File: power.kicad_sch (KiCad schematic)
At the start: 19 parts, among them J1 USB_C_Receptacle_USB2.0_16P, U1 TLV62569DBV, U3 USBLC6-2SC6, U4 SPX3819M5-L-3-3

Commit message: MCU connected
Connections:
- net MCU_USB_D+: now reaches U3.4 (I/O2)
- net MCU_USB_D-: now reaches U3.6 (I/O1)
- net +3.3V renamed +3V3
- net +3.3VA renamed +3V3A
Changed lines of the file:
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@@
 	(rectangle
 		(start 13.97 80.01)
-		(end 96.52 153.035)
+		(end 104.14 153.035)
 		(stroke
 			(width 0.254)
@@
 	)
 	(rectangle
-		(start 99.06 14.605)
+		(start 105.41 14.605)
 		(end 284.48 161.925)
 		(stroke
@@
 	(wire
 		(pts
+			(xy 83.82 104.14) (xy 86.36 104.14)
+		)
+		(stroke
+			(width 0)
+			(type default)
+		)
+	)
+	(wire
+		(pts
 			(xy 207.01 142.24) (xy 166.37 142.24)
 		)
@@
 		(pts
 			(xy 52.07 116.84) (xy 69.85 116.84)
+		)
+		(stroke
+			(width 0)
+			(type default)
+		)
+	)
+	(wire
+		(pts
+			(xy 83.82 106.68) (xy 86.36 106.68)
 		)
 		(stroke
@@
 			)
 			(justify left bottom)
+		)
+	)
+	(global_label "MCU_USB_D-"
+		(shape input)
+		(at 86.36 104.14 0)
+		(fields_autoplaced yes)
+		(effects
+			(font
+				(size 1.27 1.27)
+			)
+			(justify left)
+		)
+		(property "Intersheetrefs" "${INTERSHEET_REFS}"
+			(at 101.9847 104.14 0)
+			(effects
+				(font
+					(size 1.27 1.27)
+				)
+				(justify left)
+				(hide yes)
+			)
+		)
+	)
+	(global_label "MCU_USB_D+"
+		(shape input)
+		(at 86.36 106.68 0)
+		(fields_autoplaced yes)
+		(effects
+			(font
+				(size 1.27 1.27)
+			)
+			(justify left)
+		)
+		(property "Intersheetrefs" "${INTERSHEET_REFS}"
+			(at 101.9847 106.68 0)
+			(effects
+				(font
+					(size 1.27 1.27)
+				)
+				(justify left)
+				(hide yes)
+			)
 		)
 	)
@@
 			)
 		)
-		(property "Value" "+3.3V"
-			(at 217.17 100.33 0)
-			(effects
-				(font
-					(size 1.27 1.27)
-				)
+		(property "Value" "+3V3"
+			(at 219.71 104.1399 0)
+			(effects
+				(font
+					(size 1.27 1.27)
+				)
+				(justify left)
 			)
 		)
@@
 			)
 		)
-		(property "Value" "+3.3VA"
+		(property "Value" "+3V3A"
 			(at 196.85 43.1799 0)
 			(effects

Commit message: adding anotations
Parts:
- renumbered U1 to U7
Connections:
- net +VBUS is gone; now on net VBUS: J1.A4 (VBUS), J1.A9 (VBUS), J1.B4 (VBUS), J1.B9 (VBUS), U3.5 (VBUS)
- net GND: now also C1.2, C2.2, C3.2, C6.2, U4.2 (GND)

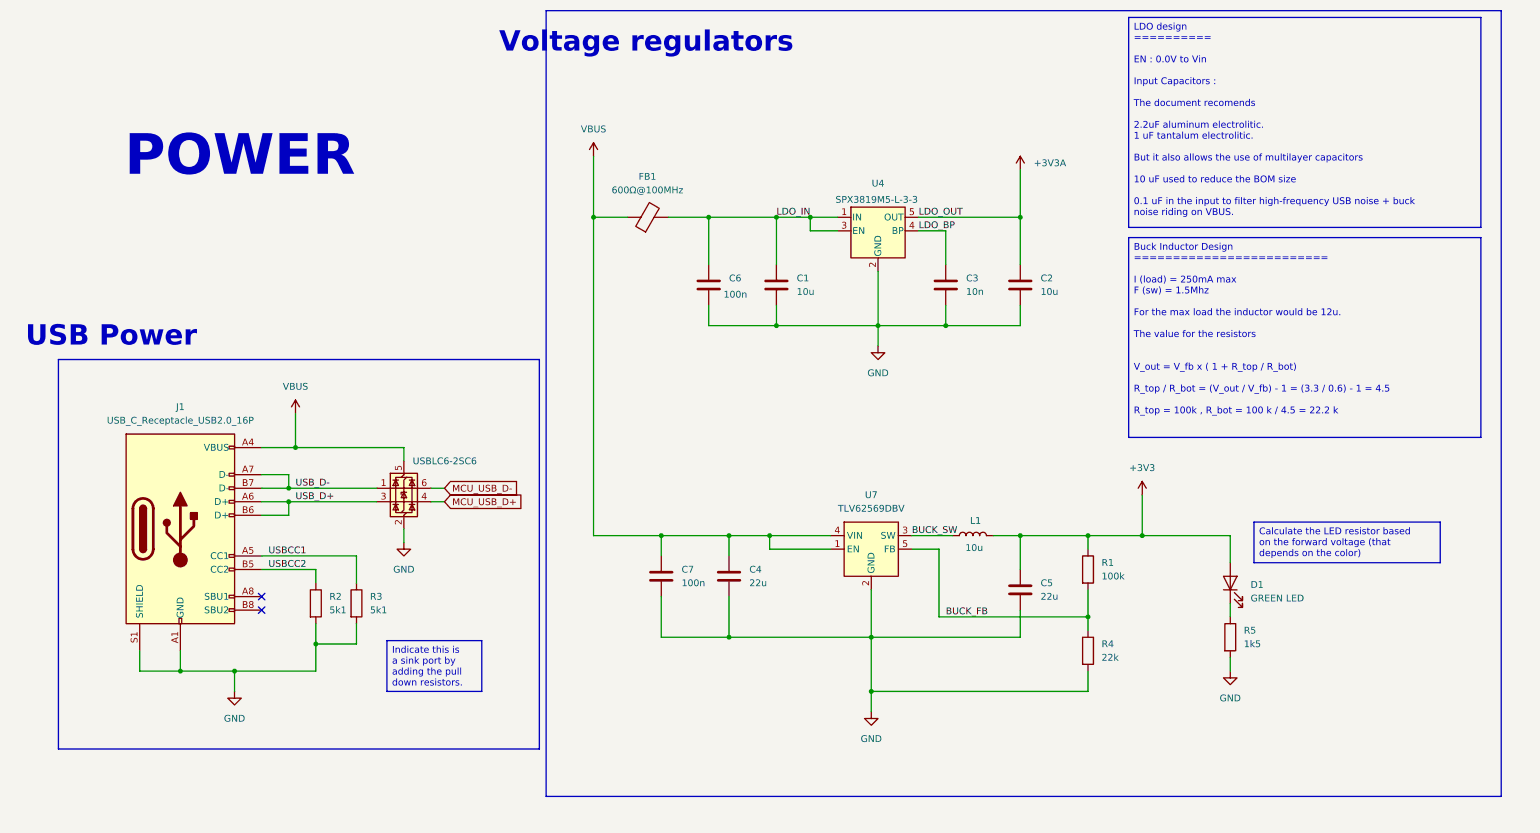
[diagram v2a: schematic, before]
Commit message: ERC fixed
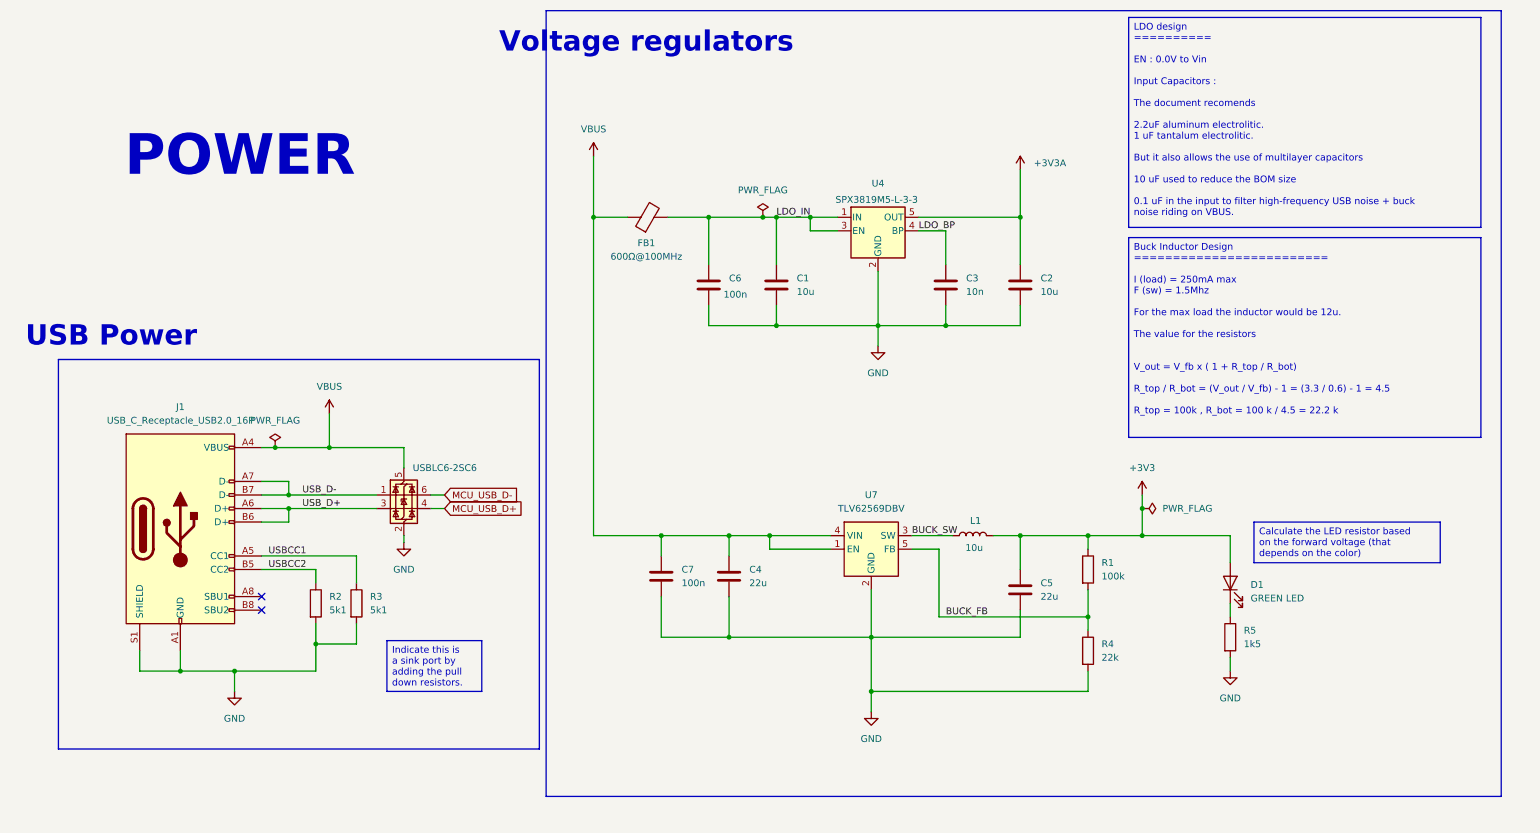
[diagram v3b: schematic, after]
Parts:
- removed J1: USB_C_Receptacle_USB2.0_16P, Connector_USB:USB_C_Receptacle_GCT_USB4105-xx-A_16P_TopMnt_Horizontal, symbol Connector:USB_C_Receptacle_USB2.0_16P
- added J1: USB_C_Receptacle_USB2.0_16P, Connector_USB:USB_C_Receptacle_GCT_USB4105-xx-A_16P_TopMnt_Horizontal, symbol Galerna:USB_C_Receptacle_USB2.0_16P
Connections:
- net GND: now also J1.A1 (GND), J1.A12 (GND), J1.B1 (GND), J1.B12 (GND), J1.S1 (SHIELD)
- net USBCC1: now also J1.A5 (CC1)
- net USBCC2: now also J1.B5 (CC2)
- net USB_D+: now also J1.A6 (D+), J1.B6 (D+)
- net USB_D-: now also J1.A7 (D-), J1.B7 (D-)
- net VBUS: now also J1.A4 (VBUS), J1.A9 (VBUS), J1.B4 (VBUS), J1.B9 (VBUS)

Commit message: footprints updated
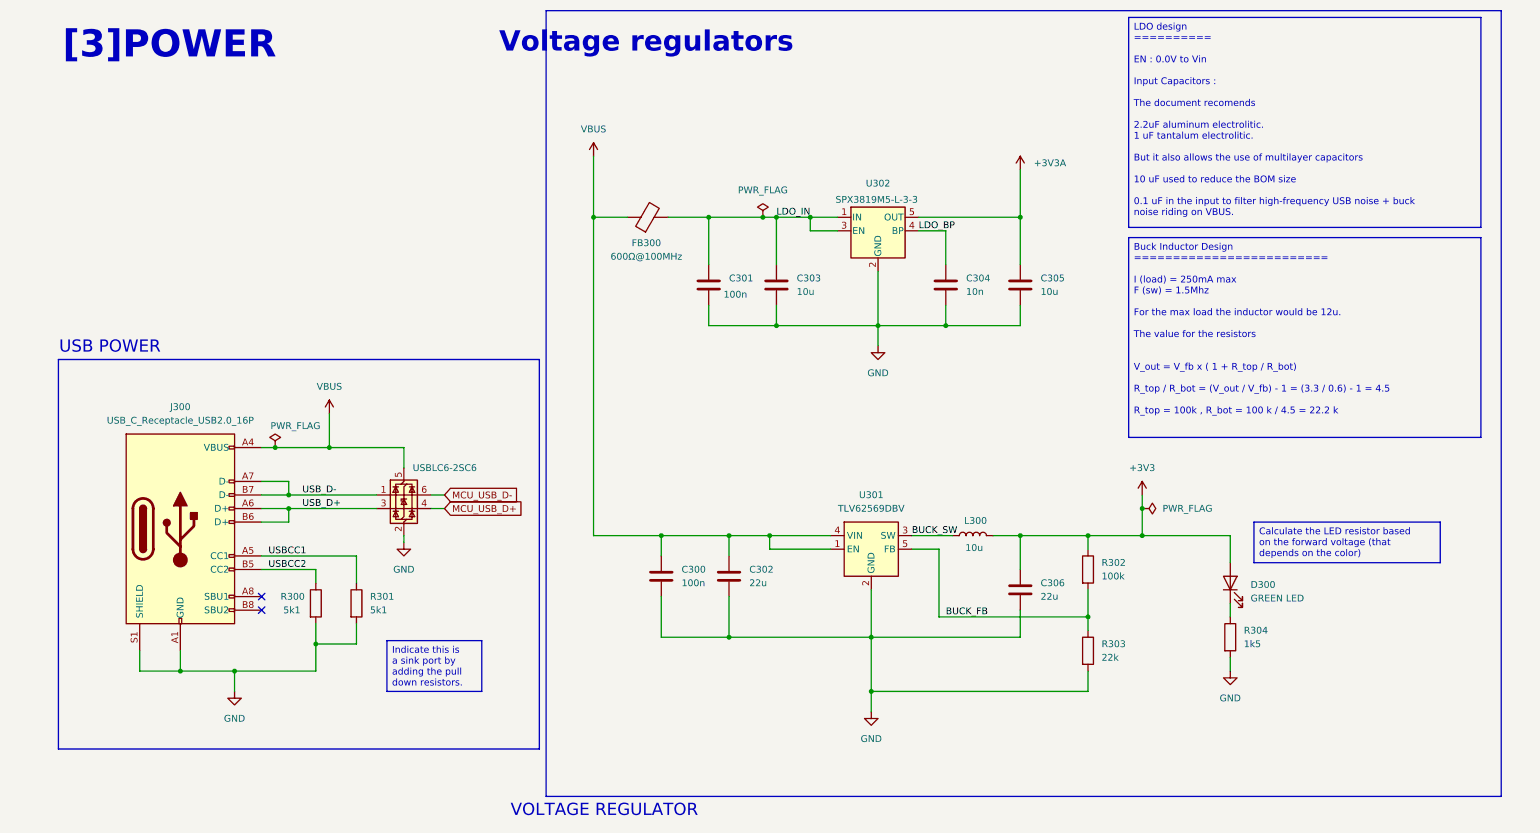
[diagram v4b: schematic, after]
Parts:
- C300: renamed from C7; footprint (none) -> Capacitor_SMD:C_0402_1005Metric
- C301: renamed from C6; footprint (none) -> Capacitor_SMD:C_0402_1005Metric
- C302: renamed from C4; footprint (none) -> Capacitor_SMD:C_0805_2012Metric
- C303: renamed from C1; footprint (none) -> Capacitor_SMD:C_0603_1608Metric
- C304: renamed from C3; footprint (none) -> Capacitor_SMD:C_0402_1005Metric
- C305: renamed from C2; footprint (none) -> Capacitor_SMD:C_0603_1608Metric
- C306: renamed from C5; footprint (none) -> Capacitor_SMD:C_0805_2012Metric
- D300: renamed from D1; footprint (none) -> LED_SMD:LED_0402_1005Metric
- L300: renamed from L1; footprint (none) -> Inductor_SMD:L_0402_1005Metric
- R300: renamed from R2; footprint (none) -> Resistor_SMD:R_0402_1005Metric
- R301: renamed from R3; footprint (none) -> Resistor_SMD:R_0402_1005Metric
- R302: renamed from R1; footprint (none) -> Resistor_SMD:R_0402_1005Metric
- R303: renamed from R4; footprint (none) -> Resistor_SMD:R_0402_1005Metric
- R304: renamed from R5; footprint (none) -> Resistor_SMD:R_0402_1005Metric
- renumbered FB1 to FB300, J1 to J300, U3 to U300, U7 to U301, U4 to U302
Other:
- note added: "USB POWER"
- note added: "VOLTAGE REGULATOR"
- note added: "[3]POWER"
- note removed: "POWER"
- note removed: "USB Power"

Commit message: footprint updated
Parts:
- L300: footprint Inductor_SMD:L_0402_1005Metric -> Inductor_SMD:L_0603_1608Metric
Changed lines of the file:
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@@
 			)
 		)
-		(property "Footprint" "Inductor_SMD:L_0402_1005Metric"
+		(property "Footprint" "Inductor_SMD:L_0603_1608Metric"
 			(at 185.42 113.03 0)
 			(effects

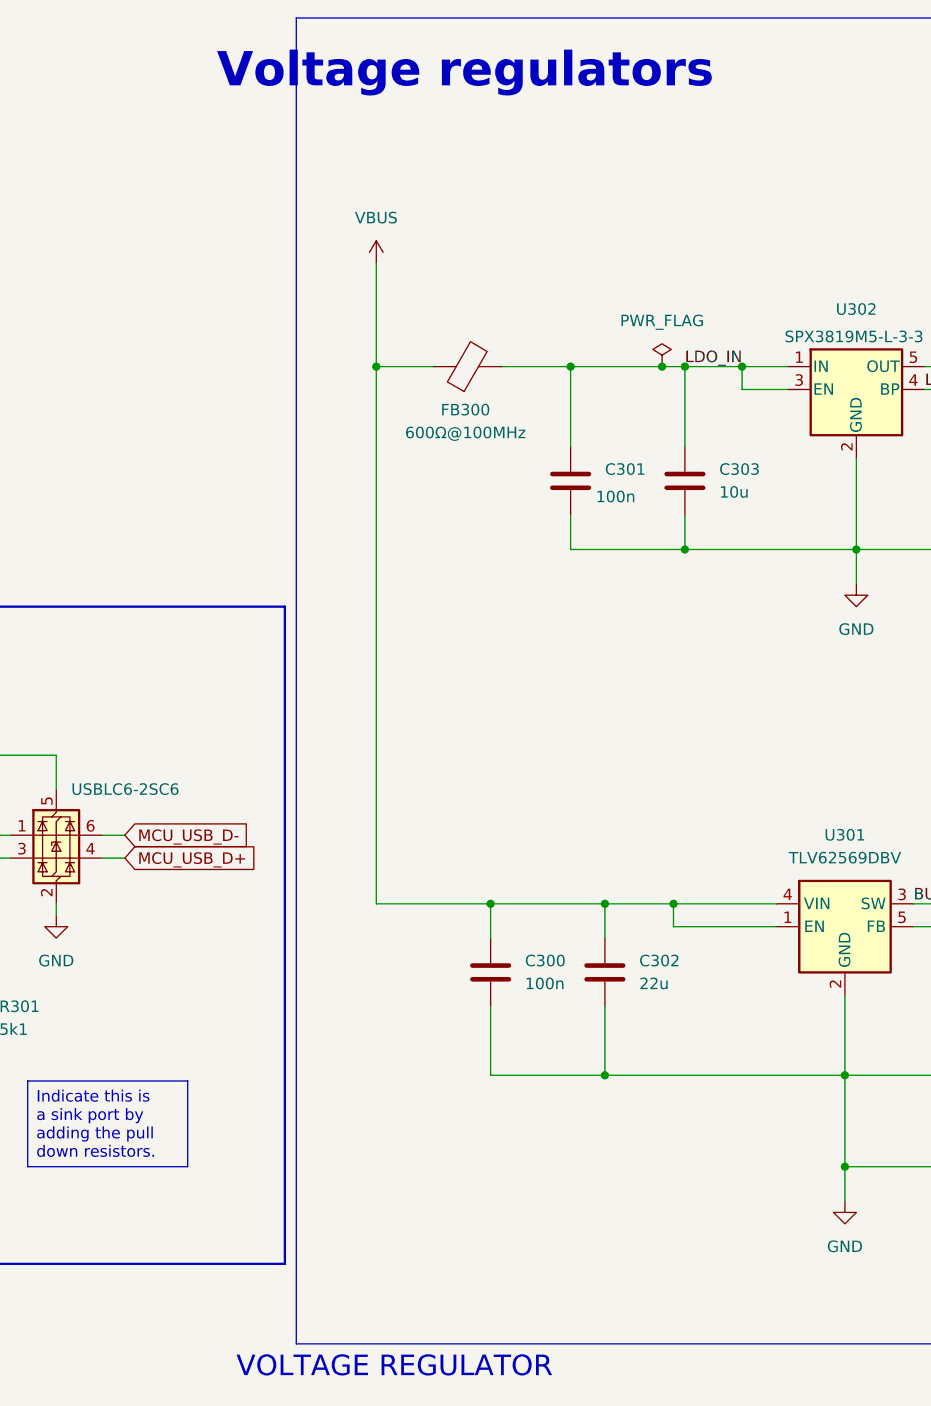
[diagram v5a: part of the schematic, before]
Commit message: codec placed
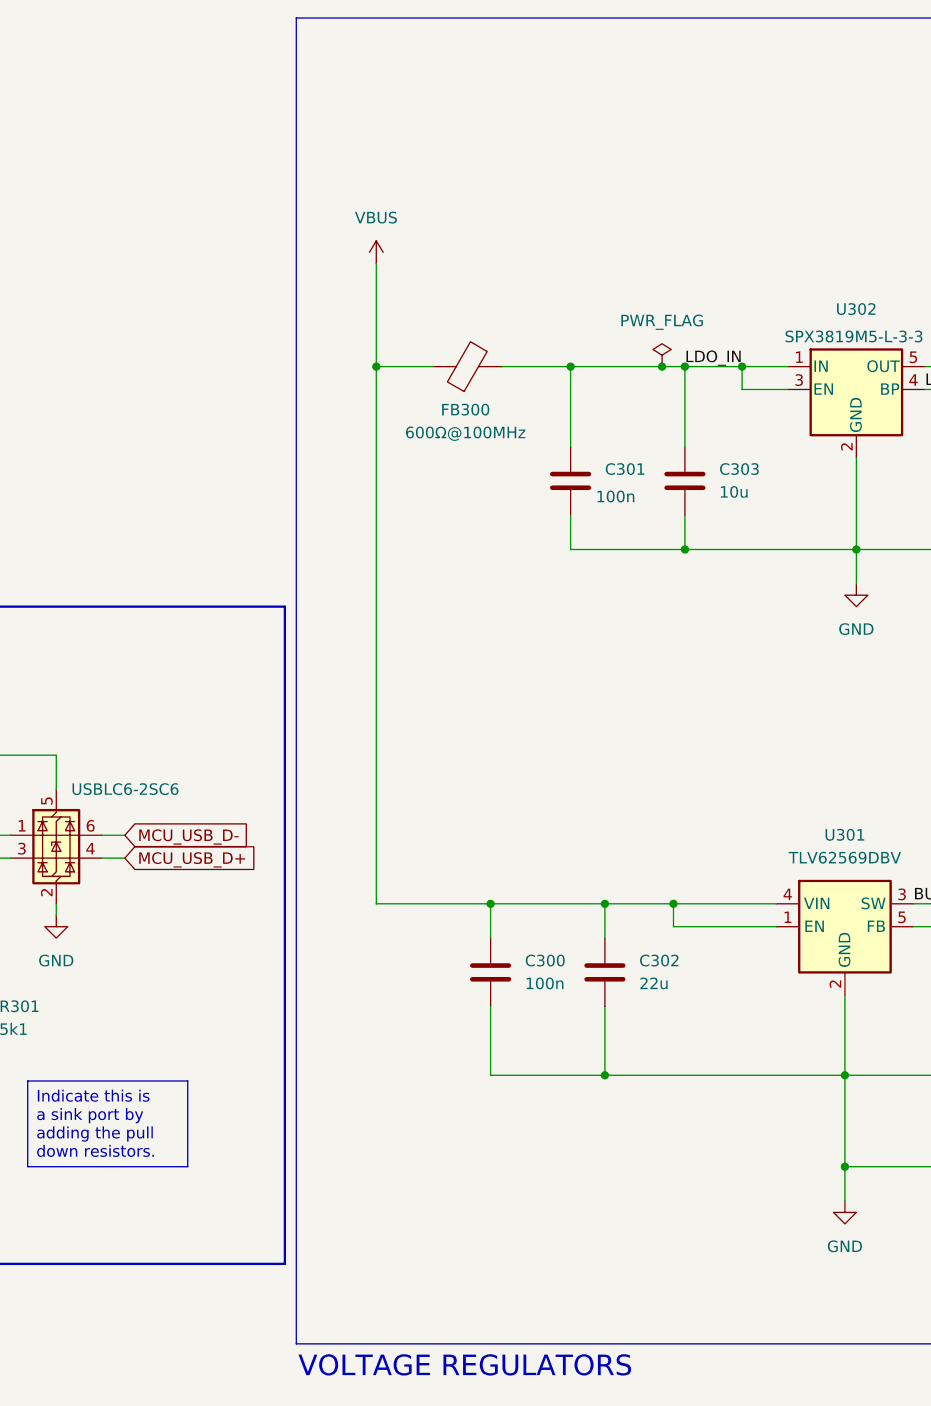
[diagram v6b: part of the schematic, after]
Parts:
- L300: footprint Inductor_SMD:L_0603_1608Metric -> Inductor_SMD:L_0805_2012Metric
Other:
- note added: "VOLTAGE REGULATORS"
- note removed: "VOLTAGE REGULATOR"
- note removed: "Voltage regulators"
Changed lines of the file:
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@@
 		)
 	)
-	(text "VOLTAGE REGULATOR"
+	(text "VOLTAGE REGULATORS"
 		(exclude_from_sim no)
-		(at 116.332 164.592 0)
+		(at 124.206 164.592 0)
 		(effects
 			(font
@@
 				(size 5.08 5.08)
 				(thickness 0.508)
-				(bold yes)
-			)
-		)
-	)
-	(text "Voltage regulators\n"
-		(exclude_from_sim no)
-		(at 124.206 20.574 0)
-		(effects
-			(font
-				(face "Fira Sans Compressed UltraLight")
-				(size 3.81 3.81)
-				(thickness 0.254)
 				(bold yes)
 			)
@@
 			)
 		)
-		(property "Footprint" "Inductor_SMD:L_0603_1608Metric"
+		(property "Footprint" "Inductor_SMD:L_0805_2012Metric"
 			(at 185.42 113.03 0)
 			(effects

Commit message: routing update
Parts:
- L300: footprint Inductor_SMD:L_0805_2012Metric -> Inductor_SMD:L_Sunlord_MWSA0618S; LCSC (none) -> C408423
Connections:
- net GND: no longer J300.S1 (SHIELD)
- no-connect marks 2 -> 3
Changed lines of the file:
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@@
-	)
-	(junction
-		(at 36.83 138.43)
-		(diameter 0)
-		(color 0 0 0 0)
 	)
 	(junction
@@
 	)
 	(no_connect
+		(at 29.21 134.62)
+	)
+	(no_connect
 		(at 52.07 127)
 	)
@@
 	(wire
 		(pts
-			(xy 29.21 134.62) (xy 29.21 138.43)
-		)
-		(stroke
-			(width 0)
-			(type default)
-		)
-	)
-	(wire
-		(pts
 			(xy 180.34 73.66) (xy 194.31 73.66)
 		)
@@
 		(pts
 			(xy 160.02 55.88) (xy 154.94 55.88)
-		)
-		(stroke
-			(width 0)
-			(type default)
-		)
-	)
-	(wire
-		(pts
-			(xy 29.21 138.43) (xy 36.83 138.43)
 		)
 		(stroke
@@
 	)
 	(global_label "MCU_USB_D-"
-		(shape input)
+		(shape bidirectional)
 		(at 86.36 105.41 0)
 		(fields_autoplaced yes)
@@
 		)
 		(property "Intersheetrefs" "${INTERSHEET_REFS}"
-			(at 101.9847 105.41 0)
+			(at 103.096 105.41 0)
 			(effects
 				(font
@@
 	)
 	(global_label "MCU_USB_D+"
-		(shape input)
+		(shape bidirectional)
 		(at 86.36 107.95 0)
 		(fields_autoplaced yes)
@@
 		)
 		(property "Intersheetrefs" "${INTERSHEET_REFS}"
-			(at 101.9847 107.95 0)
+			(at 103.096 107.95 0)
 			(effects
 				(font
@@
 			)
 		)
-		(property "Footprint" "Inductor_SMD:L_0805_2012Metric"
+		(property "Footprint" "Inductor_SMD:L_Sunlord_MWSA0618S"
 			(at 185.42 113.03 0)
 			(effects
@@
 			)
 		)
-		(property "Datasheet" "~"
+		(property "Datasheet" "https://jlcpcb.com/partdetail/Sunlord-MWSA0618S100MT/C408423"
 			(at 185.42 113.03 0)
 			(effects
@@
 			(effects
 				(font
+					(size 1.27 1.27)
+				)
+				(hide yes)
+			)
+		)
+		(property "LCSC" "C408423"
+			(at 185.42 113.03 90)
+			(effects
+				(font

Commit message: All DRC fixed
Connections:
- net GND: now also J300.S1 (SHIELD)
- no-connect marks 3 -> 2
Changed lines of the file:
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@@
+	)
+	(junction
+		(at 36.83 138.43)
+		(diameter 0)
+		(color 0 0 0 0)
 	)
 	(junction
@@
 	(no_connect
 		(at 52.07 124.46)
-	)
-	(no_connect
-		(at 29.21 134.62)
 	)
 	(no_connect
@@
 		)
 		(stroke
+			(width 0)
+			(type default)
+		)
+	)
+	(wire
+		(pts
+			(xy 29.21 138.43) (xy 36.83 138.43)
+		)
+		(stroke
+			(width 0)
+			(type default)
+		)
+	)
+	(wire
+		(pts
+			(xy 29.21 134.62) (xy 29.21 138.43)
+		)
+		(stroke
